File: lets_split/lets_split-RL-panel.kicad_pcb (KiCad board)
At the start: 2 copper layers, 229 x 78 mm, 120 parts, among them J1 3PIN, J2 CONN_01X04, J3 3PIN, SW1 SW_PUSH, SW10 SW_PUSH, SW11 SW_PUSH, SW12 SW_PUSH, SW13 SW_PUSH, SW14 SW_PUSH, SW15 SW_PUSH, SW16 SW_PUSH, SW17 SW_PUSH, SW18 SW_PUSH, SW19 SW_PUSH, SW2 SW_PUSH, SW20 SW_PUSH, SW21 SW_PUSH, SW22 SW_PUSH, SW23 SW_PUSH, SW24 SW_PUSH, SW3 SW_PUSH, SW4 SW_PUSH, SW5 SW_PUSH, SW6 SW_PUSH, SW7 SW_PUSH, SW8 SW_PUSH, SW9 SW_PUSH, U1 ArduinoProMicro

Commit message: Added zipped gerber and renders
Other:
- outline, holes or cut-outs redrawn
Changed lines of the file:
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@@
     (links 247)
     (no_connects 49)
-    (area 390.924999 12.924999 620.075001 91.075001)
+    (area 19.250001 56.062599 263.075001 143.7)
     (thickness 1.6)
-    (drawings 54)
+    (drawings 72)
     (tracks 940)
     (zones 0)
@@
       (drillshape 0)
       (scaleselection 1)
-      (outputdirectory ""))
+      (outputdirectory Gerbers/))
   )
   (net 0 "")
@@
       (net 41 "Net-(JP1-Pad2)"))
   )
+  (gr_line (start 134 64) (end 145 64) (layer Edge.Cuts) (width 0.15))
+  (gr_arc (start 261 66) (end 261 64) (angle 90) (layer Edge.Cuts) (width 0.15))
+  (gr_arc (start 261 135) (end 263 135) (angle 90) (layer Edge.Cuts) (width 0.15))
+  (gr_line (start 147 67.5) (end 147 66) (layer Edge.Cuts) (width 0.15))
+  (gr_arc (start 145 66) (end 145 64) (angle 90) (layer Edge.Cuts) (width 0.15))
+  (gr_arc (start 148.5 67.5) (end 150 67.5) (angle 180) (layer Edge.Cuts) (width 0.15))
+  (gr_line (start 150 67.5) (end 150 66) (layer Edge.Cuts) (width 0.15))
+  (gr_arc (start 152 66) (end 150 66) (angle 90) (layer Edge.Cuts) (width 0.15))
+  (gr_line (start 147 133.5) (end 147 135) (layer Edge.Cuts) (width 0.15))
+  (gr_line (start 150 133.5) (end 150 135) (layer Edge.Cuts) (width 0.15))
+  (gr_arc (start 148.5 133.5) (end 147 133.5) (angle 180) (layer Edge.Cuts) (width 0.15))
+  (gr_arc (start 152 135) (end 152 137) (angle 90) (layer Edge.Cuts) (width 0.15))
+  (gr_line (start 145 137) (end 36 137) (layer Edge.Cuts) (width 0.15))
+  (gr_arc (start 145 135) (end 147 135) (angle 90) (layer Edge.Cuts) (width 0.15))
+  (gr_arc (start 36 135) (end 36 137) (angle 90) (layer Edge.Cuts) (width 0.15))
+  (gr_arc (start 36 66) (end 34 66) (angle 90) (layer Edge.Cuts) (width 0.15))
+  (dimension 229 (width 0.3) (layer Cmts.User)
+    (gr_text "229,000 mm" (at 148.5 142.349999) (layer Cmts.User)
+      (effects (font (size 1.5 1.5) (thickness 0.3)))
+    )
+    (feature1 (pts (xy 263 137) (xy 263 143.699999)))
+    (feature2 (pts (xy 34 137) (xy 34 143.699999)))
+    (crossbar (pts (xy 34 140.999999) (xy 263 140.999999)))
+    (arrow1a (pts (xy 263 140.999999) (xy 261.873496 141.58642)))
+    (arrow1b (pts (xy 263 140.999999) (xy 261.873496 140.413578)))
+    (arrow2a (pts (xy 34 140.999999) (xy 35.126504 141.58642)))
+    (arrow2b (pts (xy 34 140.999999) (xy 35.126504 140.413578)))
+  )
+  (dimension 77.75 (width 0.3) (layer Cmts.User)
+    (gr_text "77,750 mm" (at 25.9 98.125 270) (layer Cmts.User)
+      (effects (font (size 1.5 1.5) (thickness 0.3)))
+    )
+    (feature1 (pts (xy 46.25 137) (xy 24.55 137)))
+    (feature2 (pts (xy 46.25 59.25) (xy 24.55 59.25)))
+    (crossbar (pts (xy 27.25 59.25) (xy 27.25 137)))
+    (arrow1a (pts (xy 27.25 137) (xy 26.663579 135.873496)))
+    (arrow1b (pts (xy 27.25 137) (xy 27.836421 135.873496)))
+    (arrow2a (pts (xy 27.25 59.25) (xy 26.663579 60.376504)))
+    (arrow2b (pts (xy 27.25 59.25) (xy 27.836421 60.376504)))
+  )
   (gr_text "By Wootpatoot\n" (at 203.79017 120.832402) (layer B.SilkS)
     (effects (font (size 1.5 1.5) (thickness 0.3)) (justify left mirror))
@@
     (effects (font (size 1.5 1.5) (thickness 0.3)) (justify left mirror))
   )
-  (gr_arc (start 148.5 133.5) (end 150 133.5) (angle 180) (layer Edge.Cuts) (width 0.15))
-  (gr_line (start 150 133.5) (end 150 103) (layer Edge.Cuts) (width 0.15))
-  (gr_line (start 147 103) (end 147 133.5) (layer Edge.Cuts) (width 0.15))
-  (gr_line (start 150 67.5) (end 150 98) (layer Edge.Cuts) (width 0.15))
-  (gr_line (start 147 98) (end 147 67.5) (layer Edge.Cuts) (width 0.15))
+  (gr_arc (start 148.5 128.5) (end 150 128.5) (angle 180) (layer Edge.Cuts) (width 0.15))
+  (gr_line (start 150 128.5) (end 150 103) (layer Edge.Cuts) (width 0.15))
+  (gr_line (start 147 103) (end 147 128.5) (layer Edge.Cuts) (width 0.15))
+  (gr_line (start 150 72.5) (end 150 98) (layer Edge.Cuts) (width 0.15))
+  (gr_line (start 147 98) (end 147 72.5) (layer Edge.Cuts) (width 0.15))
   (gr_arc (start 148.5 103) (end 147 103) (angle 180) (layer Edge.Cuts) (width 0.15))
   (gr_arc (start 148.5 98) (end 150 98) (angle 180) (layer Edge.Cuts) (width 0.15))
-  (gr_arc (start 148.5 67.5) (end 147 67.5) (angle 180) (layer Edge.Cuts) (width 0.15))
+  (gr_arc (start 148.5 72.5) (end 147 72.5) (angle 180) (layer Edge.Cuts) (width 0.15))
   (gr_line (start 189 59) (end 193.5 63.5) (angle 90) (layer Edge.Cuts) (width 0.15))
   (gr_line (start 193.5 63.5) (end 234.5 63.5) (angle 90) (layer Edge.Cuts) (width 0.15))
@@
   (gr_line (start 238.75 59.25) (end 251 59.25) (angle 90) (layer Edge.Cuts) (width 0.15))
   (gr_line (start 251 59.25) (end 255.75 64) (angle 90) (layer Edge.Cuts) (width 0.15))
-  (gr_line (start 255.75 64) (end 263 64) (angle 90) (layer Edge.Cuts) (width 0.15))
-  (gr_line (start 263 64) (end 263 137) (angle 90) (layer Edge.Cuts) (width 0.15))
-  (gr_line (start 263 137) (end 34 137) (angle 90) (layer Edge.Cuts) (width 0.15))
+  (gr_line (start 255.75 64) (end 261 64) (angle 90) (layer Edge.Cuts) (width 0.15))
+  (gr_line (start 263 66) (end 263 135) (angle 90) (layer Edge.Cuts) (width 0.15))
+  (gr_line (start 261 137) (end 152 137) (angle 90) (layer Edge.Cuts) (width 0.15))
   (gr_text VCC (at 253.716 64.116 315) (layer F.SilkS)
     (effects (font (size 1 1) (thickness 0.25)))
@@
     (effects (font (size 5 5) (thickness 0.3)) (justify mirror))
   )
-  (gr_line (start 134 64) (end 163 64) (layer Edge.Cuts) (width 0.15))
+  (gr_line (start 152 64) (end 163 64) (layer Edge.Cuts) (width 0.15))
   (gr_line (start 163 64) (end 168 59) (layer Edge.Cuts) (width 0.15))
   (gr_line (start 168 59) (end 189 59) (layer Edge.Cuts) (width 0.15))
@@
     (effects (font (size 1 1) (thickness 0.25)))
   )
-  (gr_line (start 34 64) (end 34 137) (angle 90) (layer Edge.Cuts) (width 0.15))
-  (gr_line (start 41.25 64) (end 34 64) (angle 90) (layer Edge.Cuts) (width 0.15))
+  (gr_line (start 34 66) (end 34 135) (angle 90) (layer Edge.Cuts) (width 0.15))
+  (gr_line (start 41.25 64) (end 36 64) (angle 90) (layer Edge.Cuts) (width 0.15))
   (gr_line (start 46 59.25) (end 41.25 64) (angle 90) (layer Edge.Cuts) (width 0.15))
   (gr_line (start 58.25 59.25) (end 46 59.25) (angle 90) (layer Edge.Cuts) (width 0.15))

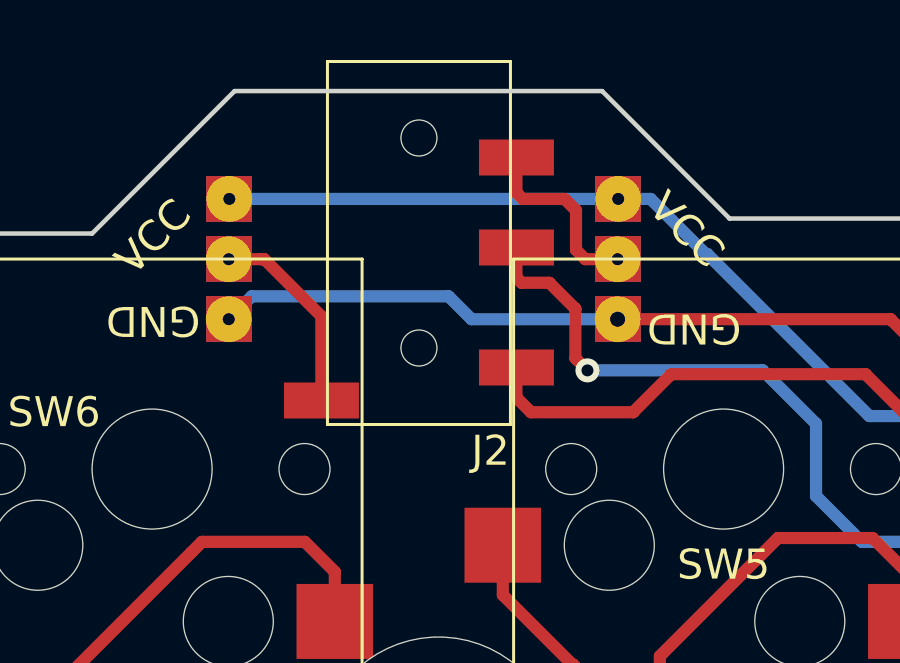
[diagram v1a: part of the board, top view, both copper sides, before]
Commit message: flipped TRRS connector the the back for both boards
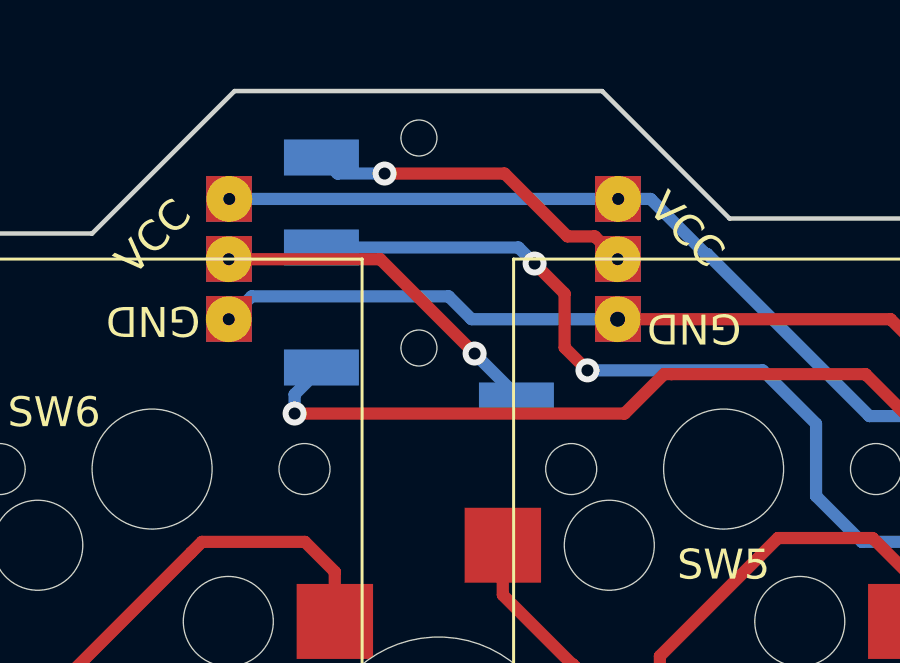
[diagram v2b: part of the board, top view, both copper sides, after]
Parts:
- J2: moved to B.Cu
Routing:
- net SCL/D3: track 174.1 -> 182.2 mm, vias 2 -> 3
- net SDA: track 181.4 -> 187.3 mm, vias 4 -> 5
- net Net-(J2-Pad4): track 12.5 -> 17.5 mm, vias 0 -> 1
- net Net-(J1-Pad2): track 13.4 -> 18.3 mm, vias 0 -> 1
